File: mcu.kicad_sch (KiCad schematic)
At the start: 23 parts, among them J13 Conn_ARM_JTAG_SWD_10, J14 Conn_01x03_Pin, J15 Conn_01x03_Pin, J16 Conn_01x02_Pin, J17 Conn_01x02_Pin, SW1 SW_Push, SW2 SW_Push, U1 STM32F407VETx, Y1 8Mhz

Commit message: added lcsc field so that bom can match during jlcpcb fab
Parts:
- C1, C2: LCSC (none) -> C1634
- C10, C11, C12, C5, C6, C7, C8, C9: LCSC (none) -> C14663
- C3, C4: LCSC (none) -> C43922
- J13: LCSC (none) -> C150517
- J14, J15: LCSC (none) -> C2894926
- J16, J17: LCSC (none) -> C3012204
- R1, R2: LCSC (none) -> C25804
- SW1, SW2: LCSC (none) -> C318884
- U1: LCSC (none) -> C28730
- Y1: LCSC (none) -> C518155
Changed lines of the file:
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@@
 			)
 		)
+		(property "LCSC" "C14663"
+			(at 173.99 26.67 0)
+			(effects
+				(font
+					(size 1.27 1.27)
+				)
+				(hide yes)
+			)
+		)
 		(pin "1"
 		)
@@
 			)
 		)
+		(property "LCSC" "C150517"
+			(at 224.79 53.34 0)
+			(effects
+				(font
+					(size 1.27 1.27)
+				)
+				(hide yes)
+			)
+		)
 		(pin "9"
 		)
@@
 			)
 		)
+		(property "LCSC" "C14663"
+			(at 189.23 26.67 0)
+			(effects
+				(font
+					(size 1.27 1.27)
+				)
+				(hide yes)
+			)
+		)
 		(pin "1"
 		)
@@
 			)
 		)
+		(property "LCSC" "C43922"
+			(at 67.31 163.83 0)
+			(effects
+				(font
+					(size 1.27 1.27)
+				)
+				(hide yes)
+			)
+		)
 		(pin "1"
 		)
@@
 			)
 		)
+		(property "LCSC" "C2894926"
+			(at 251.46 90.17 0)
+			(effects
+				(font
+					(size 1.27 1.27)
+				)
+				(hide yes)
+			)
+		)
 		(pin "1"
 		)
@@
 			)
 		)
+		(property "LCSC" "C1634"
+			(at 44.45 68.58 0)
+			(effects
+				(font
+					(size 1.27 1.27)
+				)
+				(hide yes)
+			)
+		)
 		(pin "1"
 		)
@@
 			)
 		)
+		(property "LCSC" "C14663"
+			(at 151.13 26.67 0)
+			(effects
+				(font
+					(size 1.27 1.27)
+				)
+				(hide yes)
+			)
+		)
 		(pin "1"
 		)
@@
 			)
 		)
+		(property "LCSC" "C14663"
+			(at 166.37 26.67 0)
+			(effects
+				(font
+					(size 1.27 1.27)
+				)
+				(hide yes)
+			)
+		)
 		(pin "1"
 		)
@@
 			)
 		)
+		(property "LCSC" "C14663"
+			(at 158.75 26.67 0)
+			(effects
+				(font
+					(size 1.27 1.27)
+				)
+				(hide yes)
+			)
+		)
 		(pin "1"
 		)
@@
 			)
 		)
+		(property "LCSC" "C43922"
+			(at 72.39 163.83 0)
+			(effects
+				(font
+					(size 1.27 1.27)
+				)
+				(hide yes)
+			)
+		)
 		(pin "1"
 		)
@@
 			)
 		)
+		(property "LCSC" "C14663"
+			(at 194.31 137.16 0)
+			(effects
+				(font
+					(size 1.27 1.27)
+				)
+				(hide yes)
+			)
+		)
 		(pin "1"
 		)
@@
 			)
 		)
+		(property "LCSC" "C518155"
+			(at 36.83 60.96 0)
+			(effects
+				(font
+					(size 1.27 1.27)
+				)
+				(hide yes)
+			)
+		)
 		(pin "3"
 		)
@@
 			)
 		)
+		(property "LCSC" "C14663"
+			(at 196.85 26.67 0)
+			(effects
+				(font
+					(size 1.27 1.27)
+				)
+				(hide yes)
+			)
+		)
 		(pin "1"
 		)
@@
 			)
 		)
+		(property "LCSC" "C25804"
+			(at 228.6 137.16 0)
+			(effects
+				(font
+					(size 1.27 1.27)
+				)
+				(hide yes)
+			)
+		)
 		(pin "2"
 		)
@@
 			)
 		)
+		(property "LCSC" "C2894926"
+			(at 251.46 80.01 0)
+			(effects
+				(font
+					(size 1.27 1.27)
+				)
+				(hide yes)
+			)
+		)
 		(pin "1"
 		)
@@
 			)
 		)
+		(property "LCSC" "C318884"
+			(at 204.47 132.08 0)
+			(effects
+				(font
+					(size 1.27 1.27)
+				)
+				(hide yes)
+			)
+		)
 		(pin "2"
 		)
@@
 			)
 		)
+		(property "LCSC" "C14663"
+			(at 181.61 26.67 0)
+			(effects
+				(font
+					(size 1.27 1.27)
+				)
+				(hide yes)
+			)
+		)
 		(pin "1"
 		)
@@
 			)
 		)
+		(property "LCSC" "C3012204"
+			(at 251.46 97.79 0)
+			(effects
+				(font
+					(size 1.27 1.27)
+				)
+				(hide yes)
+			)
+		)
 		(pin "2"
 		)
@@
 			)
 		)
+		(property "LCSC" "C1634"
+			(at 29.21 68.58 0)
+			(effects
+				(font
+					(size 1.27 1.27)
+				)
+				(hide yes)
+			)
+		)
 		(pin "1"
 		)
@@
 			)
 		)
+		(property "LCSC" "C3012204"
+			(at 251.46 105.41 0)
+			(effects
+				(font
+					(size 1.27 1.27)
+				)
+				(hide yes)
+			)
+		)
 		(pin "2"
 		)
@@
 			)
 		)
+		(property "LCSC" "C25804"
+			(at 194.31 128.27 0)
+			(effects
+				(font
+					(size 1.27 1.27)
+				)
+				(hide yes)
+			)
+		)
 		(pin "2"
 		)
@@
 			)
 		)
+		(property "LCSC" "C28730"
+			(at 104.14 109.22 0)
+			(effects
+				(font
+					(size 1.27 1.27)
+				)
+				(hide yes)
+			)
+		)
 		(pin "3"
 		)
@@
 			(at 238.76 132.08 0)
 			(effects
+				(font
+					(size 1.27 1.27)
+				)
+				(hide yes)
+			)
+		)
+		(property "LCSC" "C318884"
+			(at 238.76 132.08 0)
+			(effects

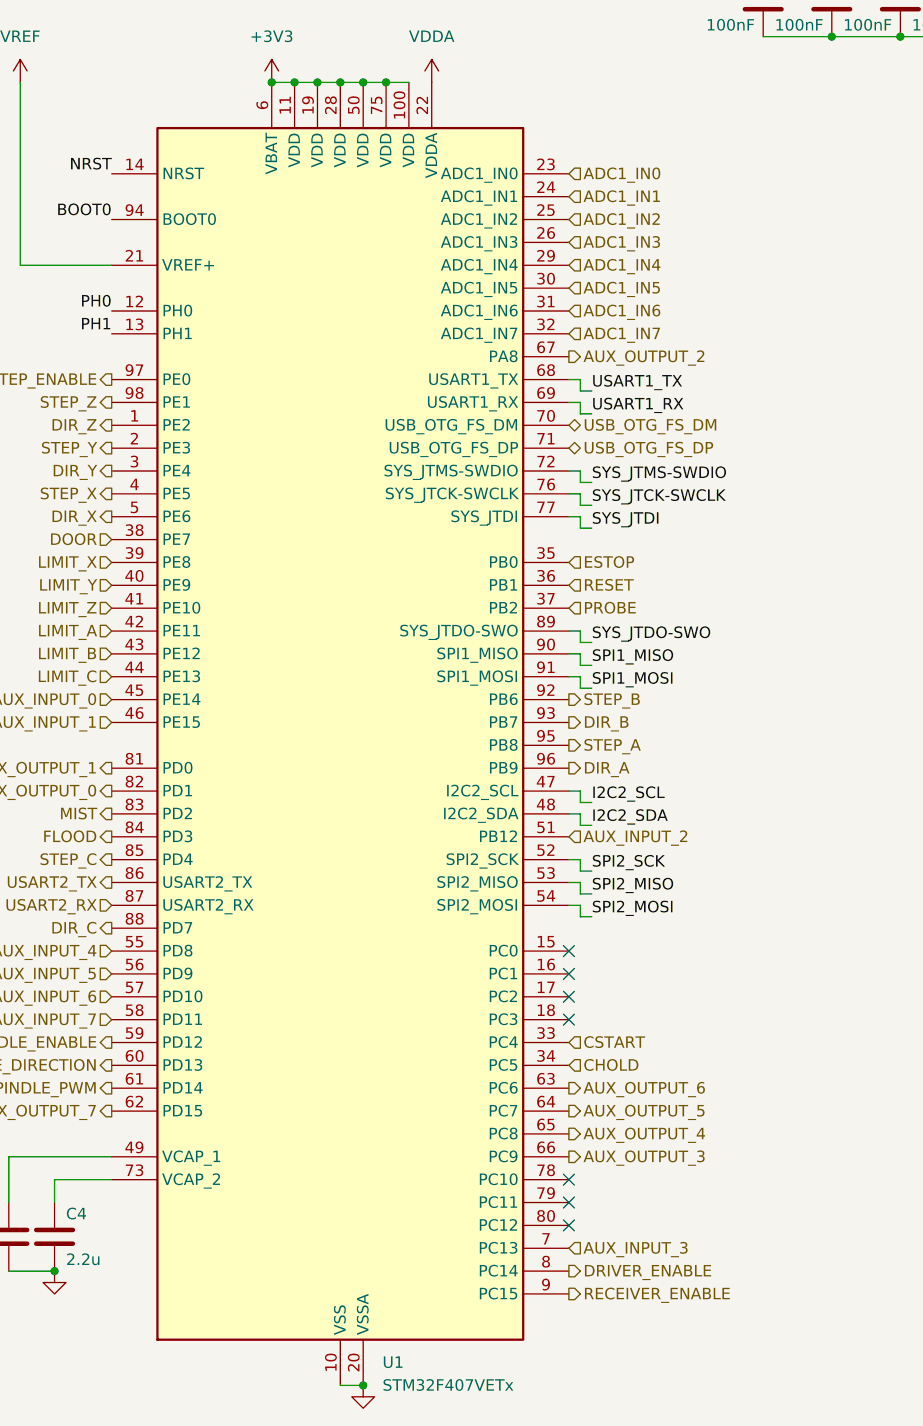
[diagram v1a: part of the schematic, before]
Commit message: moved rs485 re/de lines, start of manual
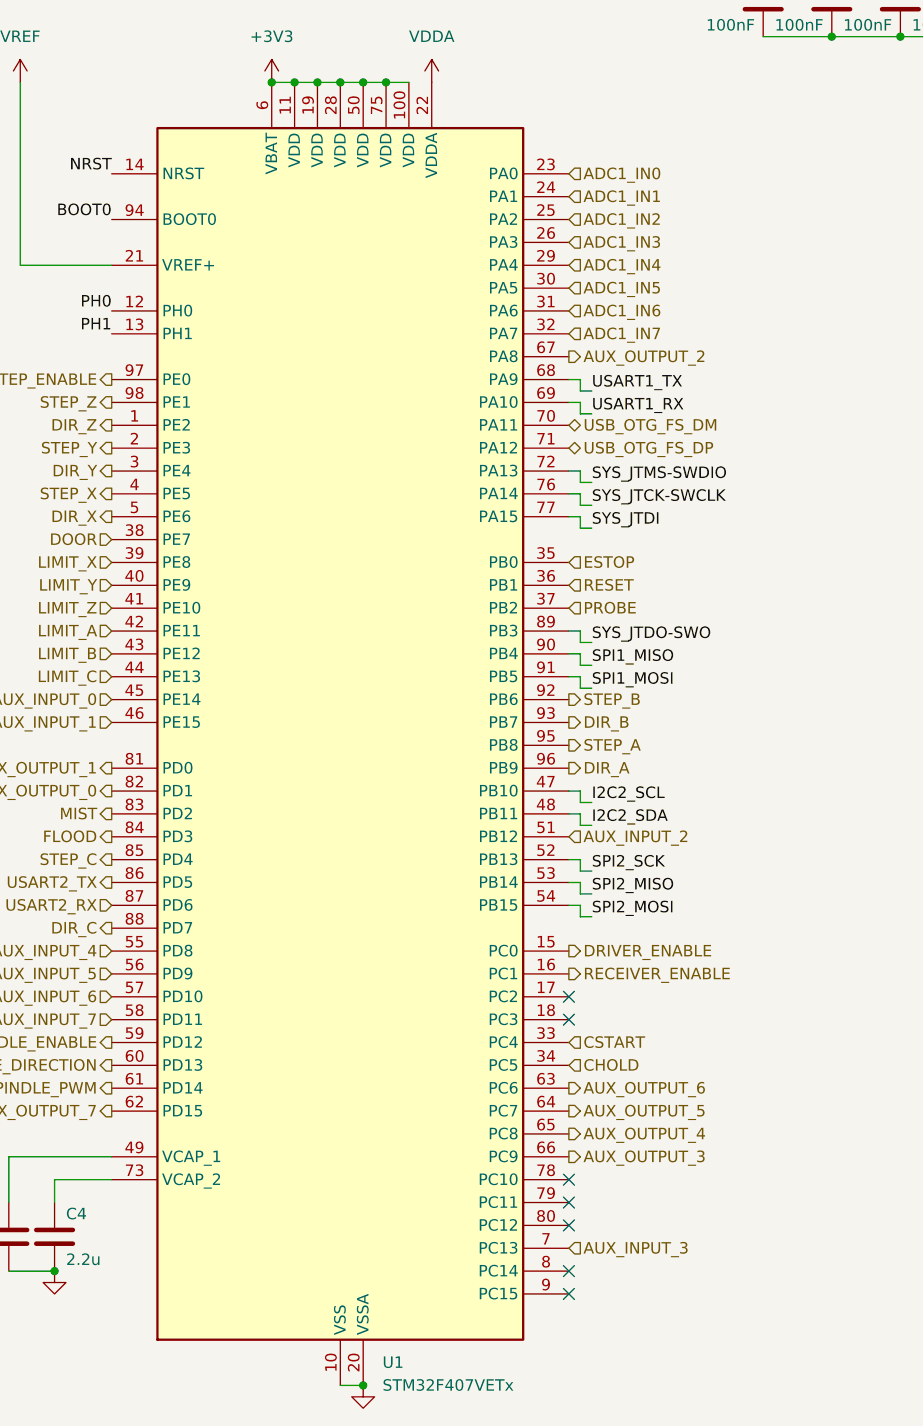
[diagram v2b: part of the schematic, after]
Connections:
- net DRIVER_ENABLE: now also U1.15 (PC0); no longer U1.8 (PC14)
- net RECEIVER_ENABLE: now also U1.16 (PC1); no longer U1.9 (PC15)
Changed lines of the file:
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@@
 	)
 	(no_connect
-		(at 129.54 134.62)
+		(at 129.54 170.18)
 	)
 	(no_connect
-		(at 129.54 132.08)
+		(at 129.54 167.64)
 	)
 	(no_connect
@@
 		)
 	)
+	(hierarchical_label "RECEIVER_ENABLE"
+		(shape output)
+		(at 129.54 134.62 0)
+		(effects
+			(font
+				(size 1.27 1.27)
+			)
+			(justify left)
+		)
+	)
 	(hierarchical_label "USB_OTG_FS_DP"
 		(shape bidirectional)
@@
 		)
 	)
-	(hierarchical_label "RECEIVER_ENABLE"
-		(shape output)
-		(at 129.54 170.18 0)
-		(effects
-			(font
-				(size 1.27 1.27)
-			)
-			(justify left)
-		)
-	)
 	(hierarchical_label "SPINDLE_ENABLE"
 		(shape output)
@@
 		)
 	)
+	(hierarchical_label "DRIVER_ENABLE"
+		(shape output)
+		(at 129.54 132.08 0)
+		(effects
+			(font
+				(size 1.27 1.27)
+			)
+			(justify left)
+		)
+	)
 	(hierarchical_label "AUX_OUTPUT_5"
 		(shape output)
@@
 		)
 	)
-	(hierarchical_label "DRIVER_ENABLE"
-		(shape output)
-		(at 129.54 167.64 0)
-		(effects
-			(font
-				(size 1.27 1.27)
-			)
-			(justify left)
-		)
-	)
 	(hierarchical_label "DIR_Z"
 		(shape output)
@@
 		)
 		(pin "70"
-			(alternate "USB_OTG_FS_DM")
 		)
 		(pin "8"
@@
 		)
 		(pin "54"
-			(alternate "SPI2_MOSI")
 		)
 		(pin "43"
@@
 		)
 		(pin "67"
-			(alternate "PA8")
 		)
 		(pin "64"
@@
 		)
 		(pin "89"
-			(alternate "SYS_JTDO-SWO")
 		)
 		(pin "55"
@@
 		)
 		(pin "30"
-			(alternate "ADC1_IN5")
 		)
 		(pin "85"
@@
 		)
 		(pin "32"
-			(alternate "ADC1_IN7")
 		)
 		(pin "51"
 		)
 		(pin "87"
-			(alternate "USART2_RX")
 		)
 		(pin "78"
@@
 		)
 		(pin "52"
-			(alternate "SPI2_SCK")
 		)
 		(pin "76"
-			(alternate "SYS_JTCK-SWCLK")
 		)
 		(pin "68"
-			(alternate "USART1_TX")
 		)
 		(pin "5"
 		)
 		(pin "24"
-			(alternate "ADC1_IN1")
 		)
 		(pin "66"
@@
 		)
 		(pin "26"
-			(alternate "ADC1_IN3")
 		)
 		(pin "63"
@@
 		)
 		(pin "48"
-			(alternate "I2C2_SDA")
 		)
 		(pin "57"
 		)
 		(pin "47"
-			(alternate "I2C2_SCL")
 		)
 		(pin "11"
@@
 		)
 		(pin "31"
-			(alternate "ADC1_IN6")
 		)
 		(pin "23"
-			(alternate "ADC1_IN0")
 		)
 		(pin "33"
@@
 		)
 		(pin "77"
-			(alternate "SYS_JTDI")
 		)
 		(pin "45"
@@
 		)
 		(pin "71"
-			(alternate "USB_OTG_FS_DP")
 		)
 		(pin "18"
 		)
 		(pin "53"
-			(alternate "SPI2_MISO")
 		)
 		(pin "79"
@@
 		)
 		(pin "86"
-			(alternate "USART2_TX")
 		)
 		(pin "50"
 		)
 		(pin "91"
-			(alternate "SPI1_MOSI")
 		)
 		(pin "12"
@@
 		)
 		(pin "29"
-			(alternate "ADC1_IN4")
 		)
 		(pin "69"
-			(alternate "USART1_RX")
 		)
 		(pin "72"
-			(alternate "SYS_JTMS-SWDIO")
 		)
 		(pin "100"
@@
 		)
 		(pin "25"
-			(alternate "ADC1_IN2")
 		)
 		(pin "90"
-			(alternate "SPI1_MISO")
 		)
 		(pin "40"

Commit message: added mating push in connectors to BOM
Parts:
- J13: # C150517 -> (none); LCSC C150517 -> C6332249
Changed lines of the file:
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@@
 			)
 		)
-		(property "Datasheet" "https://datasheet.lcsc.com/lcsc/2304140030_Amphenol-ICC-20021121-00010C4LF_C150517.pdf?_gl=1*4jlz8i*_ga*MTA5OTM3NDU3Ny4xNzE3ODEwNDk4*_ga_98M84MKSZH*MTcxODA3ODI1MC4xOS4xLjE3MTgwODg4ODUuNjAuMC4w"
+		(property "Datasheet" "https://lcsc.com/datasheet/lcsc_datasheet_2410121701_Hanbo-Electronic-HB-PH9-12725PB2GOB_C6332249.pdf"
 			(at 215.9 85.09 90)
 			(effects
@@
 			)
 		)
-		(property "Description" "Brick nogging 10P 1.27mm 双排 Black Copper Alloy 2x5P 1.27mm SMD,P=1.27mm Pin Headers ROHS"
+		(property "Description" "Gold 250V 1A Pin Header 1mm 10P 4mm -40℃~+105℃ 1.27mm Brass 2 Black 1.27mm 2x5P SMD,P=1.27mm Pin Headers ROHS"
 			(at 224.79 53.34 0)
 			(effects
@@
 			)
 		)
-		(property "#" "C150517"
+		(property "#" ""
 			(at 224.79 53.34 0)
 			(effects
@@
 			)
 		)
-		(property "LCSC" "C150517"
+		(property "LCSC" "C6332249"
 			(at 224.79 53.34 0)
 			(effects
